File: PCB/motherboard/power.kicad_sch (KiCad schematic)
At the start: 40 parts, among them U1 TPS54140ADGQR, U2 PTPS259830LNRGER, U3 AP2112K-3.3TRG1

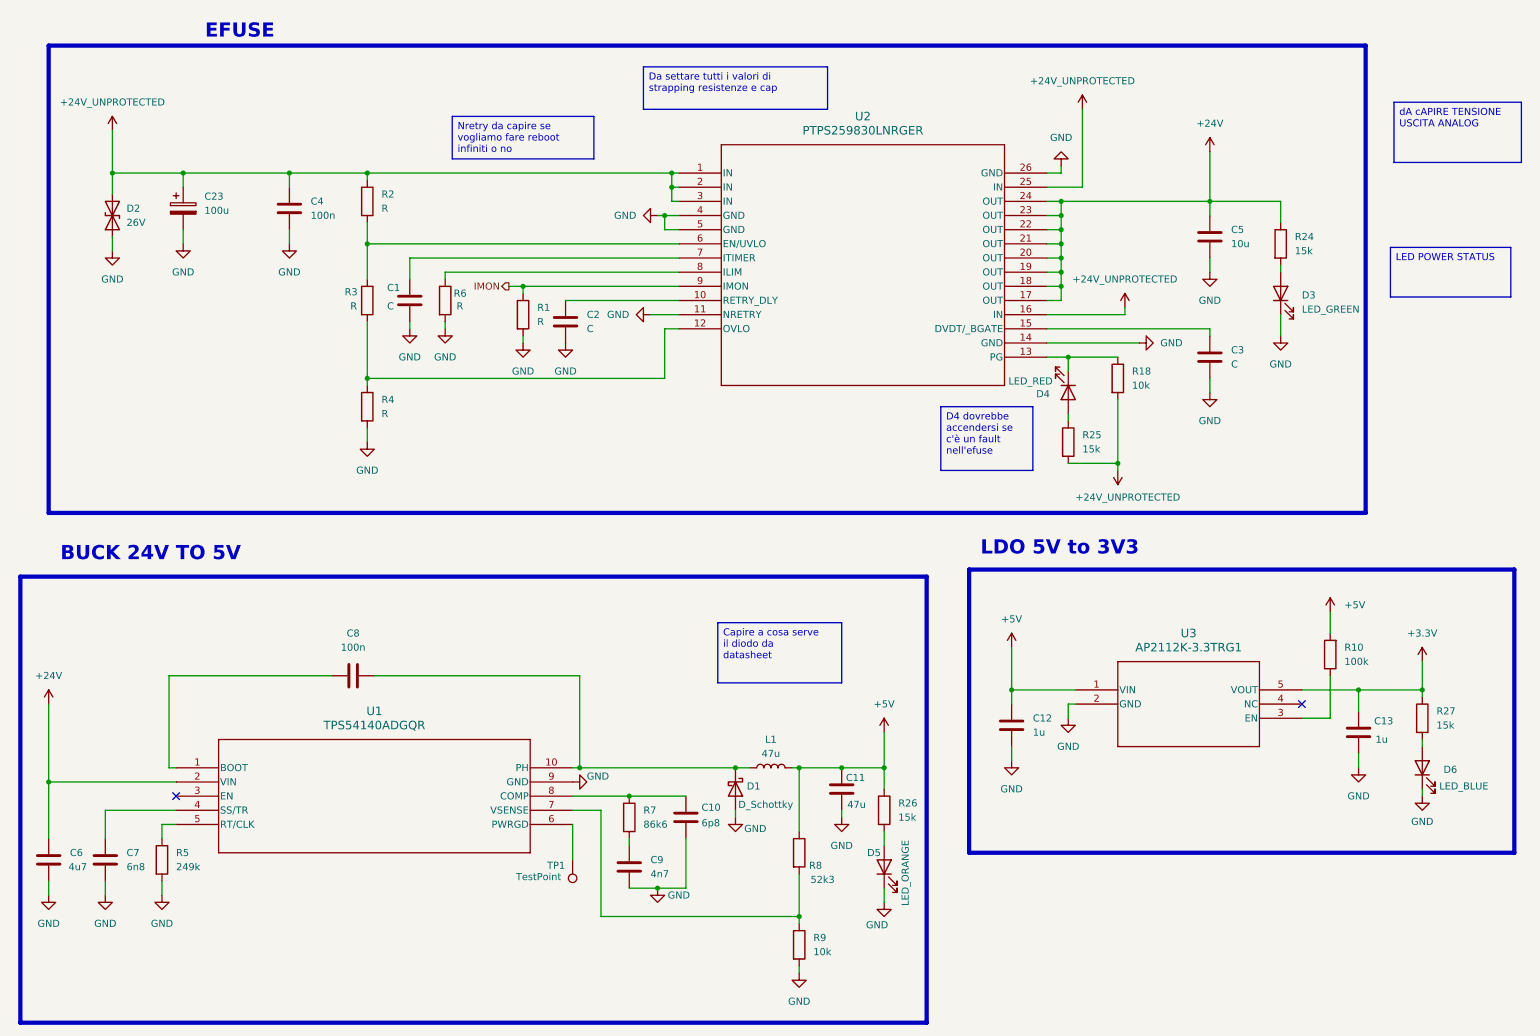
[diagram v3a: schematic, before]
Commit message: schematics need only sizing
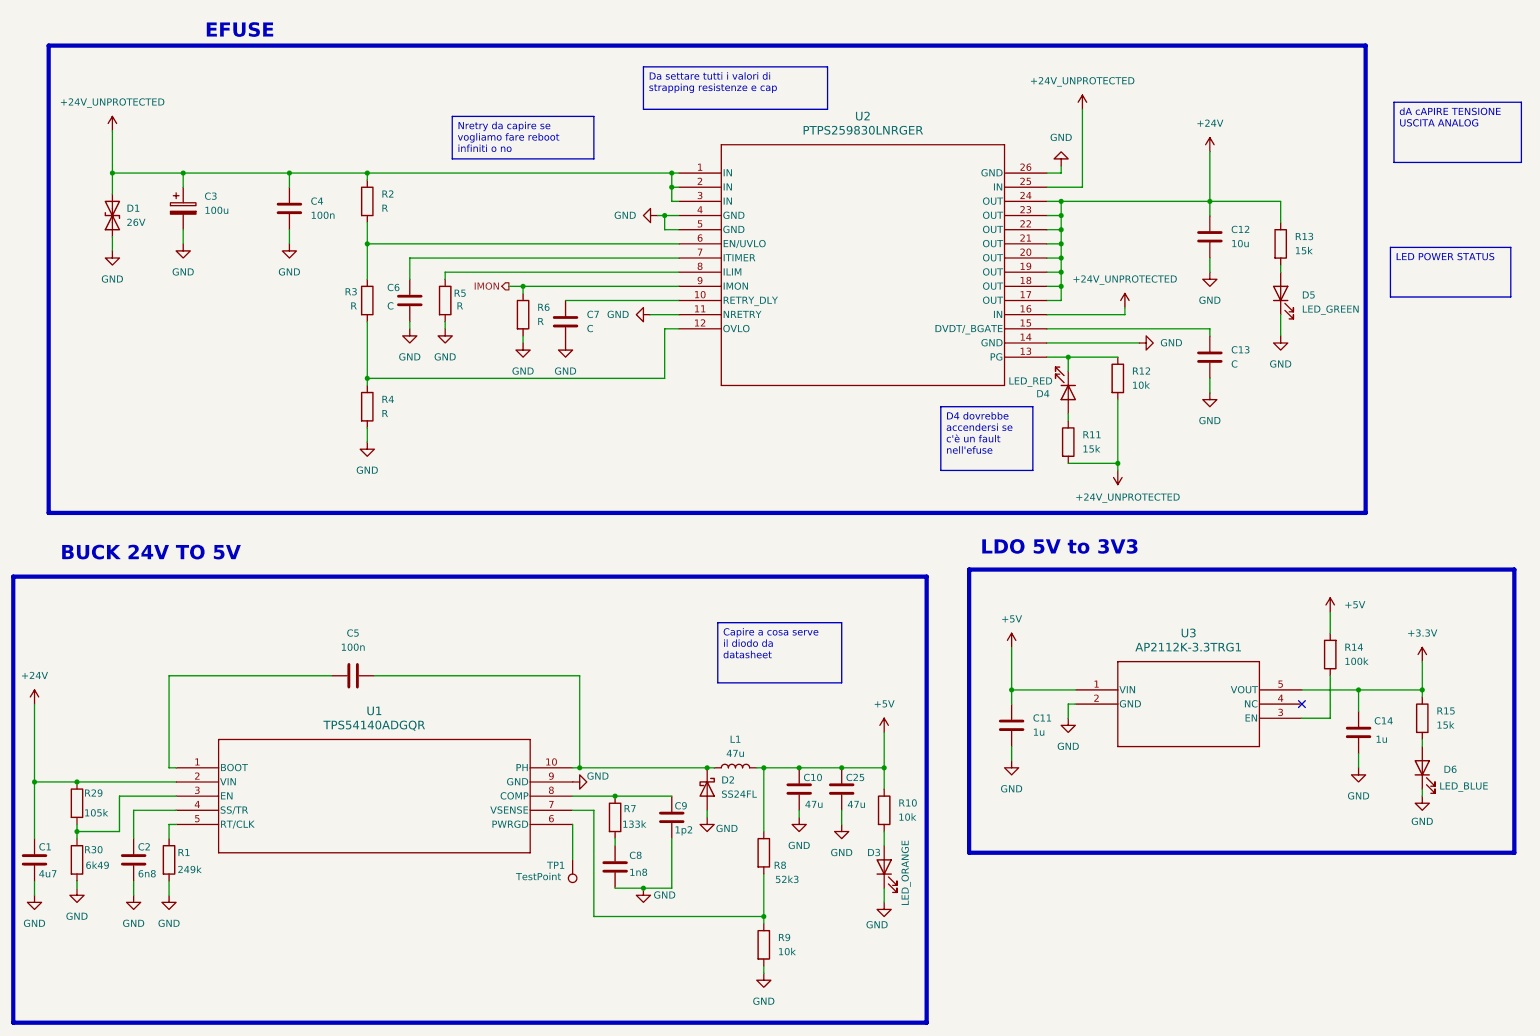
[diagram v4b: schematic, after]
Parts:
- removed D1: D_Schottky, symbol Device:D_Schottky
- added C25: 47u, Capacitor_SMD:C_1206_3216Metric_Pad1.33x1.80mm_HandSolder, symbol Device:C
- added D2: SS24FL, Diode_SMD:D_SMA, symbol Diode:SS24
- added R29: 105k, Resistor_SMD:R_1206_3216Metric_Pad1.30x1.75mm_HandSolder, symbol Device:R
- added R30: 6k49, Resistor_SMD:R_1206_3216Metric_Pad1.30x1.75mm_HandSolder, symbol Device:R
- C1: renamed from C6; footprint (none) -> Capacitor_SMD:C_1206_3216Metric_Pad1.33x1.80mm_HandSolder
- C10: renamed from C11; footprint (none) -> Capacitor_SMD:C_1206_3216Metric_Pad1.33x1.80mm_HandSolder
- C11: renamed from C12; footprint (none) -> Capacitor_SMD:C_1206_3216Metric_Pad1.33x1.80mm_HandSolder
- C12: renamed from C5; footprint (none) -> Capacitor_SMD:C_1206_3216Metric_Pad1.33x1.80mm_HandSolder
- C13: renamed from C3; footprint (none) -> Capacitor_SMD:C_1206_3216Metric_Pad1.33x1.80mm_HandSolder
- C14: renamed from C13; footprint (none) -> Capacitor_SMD:C_1206_3216Metric_Pad1.33x1.80mm_HandSolder
- C2: renamed from C7; footprint (none) -> Capacitor_SMD:C_1206_3216Metric_Pad1.33x1.80mm_HandSolder
- C3: renamed from C23; footprint (none) -> Capacitor_SMD:C_1206_3216Metric_Pad1.33x1.80mm_HandSolder
- C4: footprint (none) -> Capacitor_SMD:C_1206_3216Metric_Pad1.33x1.80mm_HandSolder
- C5: renamed from C8; footprint (none) -> Capacitor_SMD:C_1206_3216Metric_Pad1.33x1.80mm_HandSolder
- C6: renamed from C1; footprint (none) -> Capacitor_SMD:C_1206_3216Metric_Pad1.33x1.80mm_HandSolder
- C7: renamed from C2; footprint (none) -> Capacitor_SMD:C_1206_3216Metric_Pad1.33x1.80mm_HandSolder
- C8: renamed from C9; value 4n7 -> 1n8; footprint (none) -> Capacitor_SMD:C_1206_3216Metric_Pad1.33x1.80mm_HandSolder
- C9: renamed from C10; value 6p8 -> 1p2; footprint (none) -> Capacitor_SMD:C_1206_3216Metric_Pad1.33x1.80mm_HandSolder
- D3: renamed from D5; footprint (none) -> LED_SMD:LED_1206_3216Metric_Pad1.42x1.75mm_HandSolder
- D4, D6: footprint (none) -> LED_SMD:LED_1206_3216Metric_Pad1.42x1.75mm_HandSolder
- D5: renamed from D3; footprint (none) -> LED_SMD:LED_1206_3216Metric_Pad1.42x1.75mm_HandSolder
- R1: renamed from R5; footprint (none) -> Resistor_SMD:R_1206_3216Metric_Pad1.30x1.75mm_HandSolder
- R10: renamed from R26; value 15k -> 10k; footprint (none) -> Resistor_SMD:R_1206_3216Metric_Pad1.30x1.75mm_HandSolder
- R11: renamed from R25; footprint (none) -> Resistor_SMD:R_1206_3216Metric_Pad1.30x1.75mm_HandSolder
- R12: renamed from R18; footprint (none) -> Resistor_SMD:R_1206_3216Metric_Pad1.30x1.75mm_HandSolder
- R13: renamed from R24; footprint (none) -> Resistor_SMD:R_1206_3216Metric_Pad1.30x1.75mm_HandSolder
- R14: renamed from R10; footprint (none) -> Resistor_SMD:R_1206_3216Metric_Pad1.30x1.75mm_HandSolder
- R15: renamed from R27; footprint (none) -> Resistor_SMD:R_1206_3216Metric_Pad1.30x1.75mm_HandSolder
- R2, R3, R4, R8, R9: footprint (none) -> Resistor_SMD:R_1206_3216Metric_Pad1.30x1.75mm_HandSolder
- R5: renamed from R6; footprint (none) -> Resistor_SMD:R_1206_3216Metric_Pad1.30x1.75mm_HandSolder
- R6: renamed from R1; footprint (none) -> Resistor_SMD:R_1206_3216Metric_Pad1.30x1.75mm_HandSolder
- R7: value 86k6 -> 133k; footprint (none) -> Resistor_SMD:R_1206_3216Metric_Pad1.30x1.75mm_HandSolder
- TP1: footprint (none) -> TestPoint:TestPoint_Pad_D2.5mm
- U1: footprint DGQ10_1P88X1P57_TEX -> dgq10:DGQ10_1P88X1P57_TEX
- U2: footprint VQFN24_RGE_TEX -> vqfn24:VQFN24_RGE_TEX
- U3: footprint SOT_RG1_DIO -> SOT_RG1:SOT_RG1_DIO
- renumbered D2 to D1
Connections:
- net +24V: now also R29.1
- net +5V: now also C25.1
- net GND: now also C25.2, D2.2 (A), R30.2
- net at C5.2, L1.1, U1.10 (PH): now also D2.1 (K)
- net at U1.3 (EN): now also R29.2, R30.1
- no-connect marks 2 -> 1
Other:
- moved on the sheet: C1, C10, C2, C8, C9, L1, R1, R7, R8, R9

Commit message: sizing schematics done
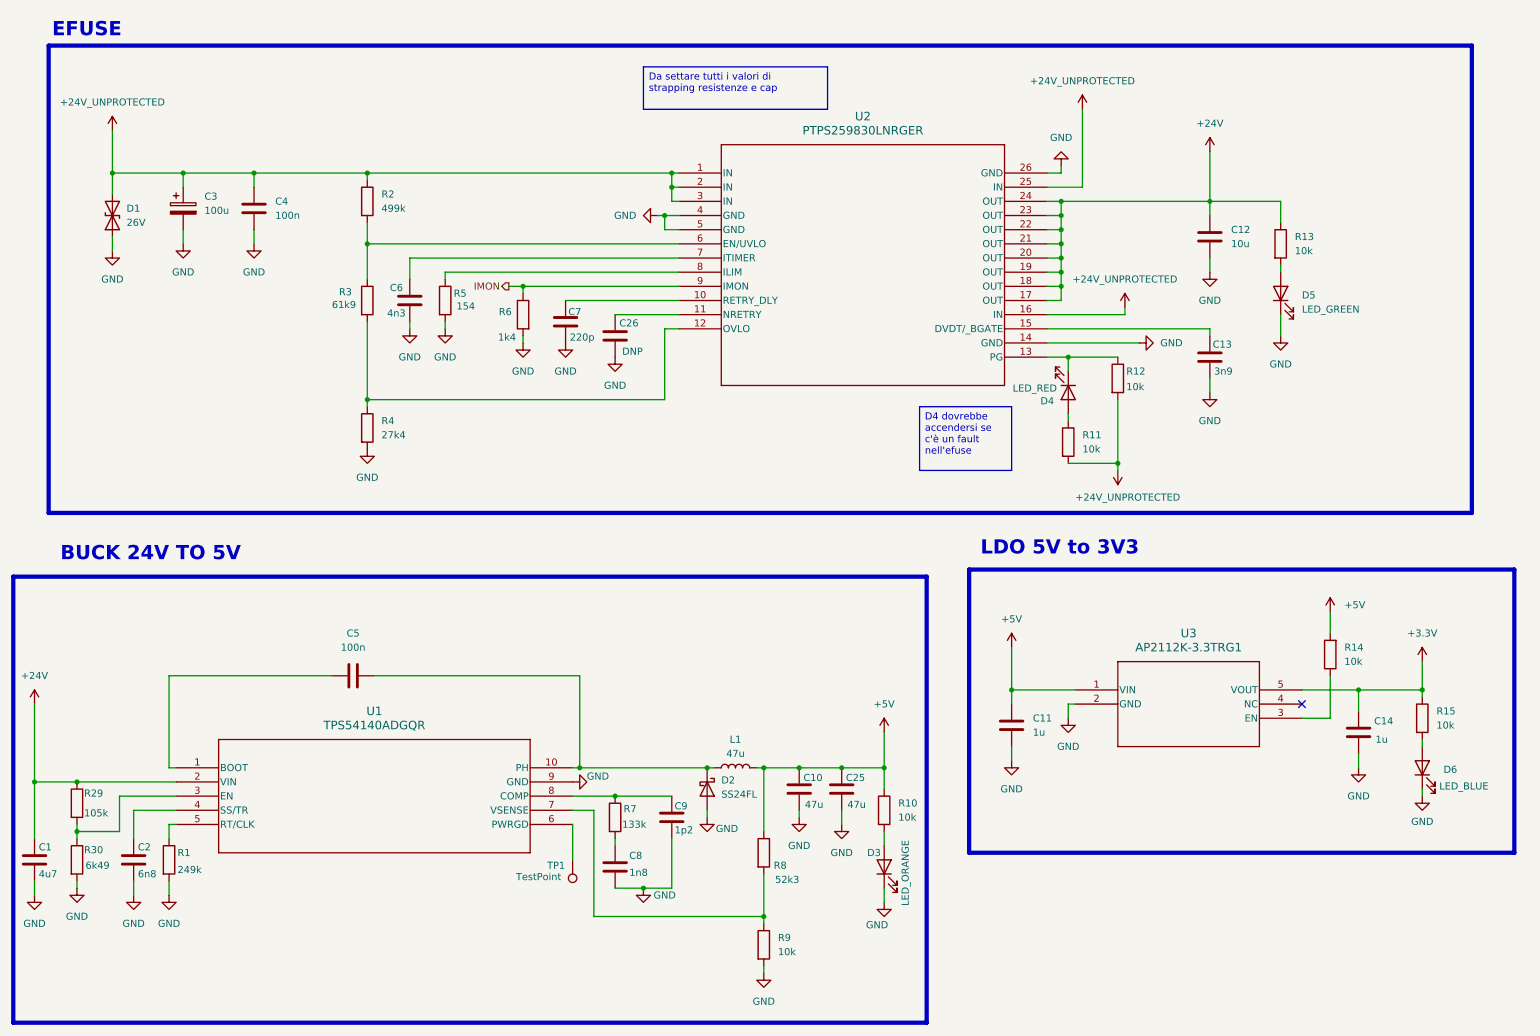
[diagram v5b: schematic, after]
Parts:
- added C26: DNP, Capacitor_SMD:C_1206_3216Metric_Pad1.33x1.80mm_HandSolder, symbol Device:C
- C13: value C -> 3n9
- C6: value C -> 4n3
- C7: value C -> 220p
- R11, R13, R15: value 15k -> 10k
- R14: value 100k -> 10k
- R2: value R -> 499k
- R3: value R -> 61k9
- R4: value R -> 27k4
- R5: value R -> 154
- R6: value R -> 1k4
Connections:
- net GND: now also C26.2; no longer U2.11 (NRETRY)
- new net: C26.1, U2.11 (NRETRY)
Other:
- moved on the sheet: C4, R4

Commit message: added last footprint on sch
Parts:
- D1: footprint (none) -> diodes:SMB_L4.3-W3.6-LS5.4-BI
- D2: footprint Diode_SMD:D_SMA -> diodes:SMA_L4.4-W2.8-LS5.4-RD
- L1: footprint (none) -> inductors:IND-SMD_L7.3-W6.8
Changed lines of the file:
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@@
 			)
 		)
-		(property "Footprint" ""
+		(property "Footprint" "inductors:IND-SMD_L7.3-W6.8"
 			(at 142.24 147.32 0)
 			(hide yes)
@@
 			)
 		)
-		(property "Footprint" "Diode_SMD:D_SMA"
+		(property "Footprint" "diodes:SMA_L4.4-W2.8-LS5.4-RD"
 			(at 132.715 151.13 0)
 			(hide yes)
@@
 			)
 		)
-		(property "Footprint" ""
+		(property "Footprint" "diodes:SMB_L4.3-W3.6-LS5.4-BI"
 			(at 30.48 48.26 0)
 			(hide yes)

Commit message: pcb layout
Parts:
- C1, C12, C13, C2, C26, C4, C5, C6, C7, C8, C9: VRATE (none) -> 50
- C10, C25: VRATE (none) -> 10
- C11, C14: VRATE (none) -> 16
- C3: footprint Capacitor_SMD:C_1206_3216Metric_Pad1.33x1.80mm_HandSolder -> Capacitor_SMD:C_Elec_10x10.2; VRATE (none) -> 50
- L1: footprint inductors:IND-SMD_L7.3-W6.8 -> inductors:IND-SMD_L13.5-W12.6_125CDMCC-DS
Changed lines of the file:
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@@
 			)
 		)
+		(property "VRATE" "50"
+			(at 34.29 163.83 0)
+			(hide yes)
+			(show_name no)
+			(do_not_autoplace no)
+			(effects
+				(font
+					(size 1.27 1.27)
+				)
+			)
+		)
 		(pin "2"
 		)
@@
 			)
 		)
+		(property "VRATE" "50"
+			(at 16.51 163.83 0)
+			(hide yes)
+			(show_name no)
+			(do_not_autoplace no)
+			(effects
+				(font
+					(size 1.27 1.27)
+				)
+			)
+		)
 		(pin "2"
 		)
@@
 			)
 		)
+		(property "VRATE" "50"
+			(at 73.66 130.81 90)
+			(hide yes)
+			(show_name no)
+			(do_not_autoplace no)
+			(effects
+				(font
+					(size 1.27 1.27)
+				)
+			)
+		)
 		(pin "1"
 		)
@@
 			)
 		)
+		(property "VRATE" "50"
+			(at 55.88 46.99 0)
+			(hide yes)
+			(show_name no)
+			(do_not_autoplace no)
+			(effects
+				(font
+					(size 1.27 1.27)
+				)
+			)
+		)
 		(pin "2"
 		)
@@
 			)
 		)
-		(property "Footprint" "Capacitor_SMD:C_1206_3216Metric_Pad1.33x1.80mm_HandSolder"
+		(property "Footprint" "Capacitor_SMD:C_Elec_10x10.2"
 			(at 44.1452 50.8 0)
 			(hide yes)
@@
 			)
 		)
+		(property "VRATE" "50"
+			(at 43.18 46.99 0)
+			(hide yes)
+			(show_name no)
+			(do_not_autoplace no)
+			(effects
+				(font
+					(size 1.27 1.27)
+				)
+			)
+		)
 		(pin "2"
 		)
@@
 			)
 		)
-		(property "Footprint" "inductors:IND-SMD_L7.3-W6.8"
+		(property "Footprint" "inductors:IND-SMD_L13.5-W12.6_125CDMCC-DS"
 			(at 142.24 147.32 0)
 			(hide yes)
@@
 			)
 		)
+		(property "VRATE" "16"
+			(at 191.77 139.7 0)
+			(hide yes)
+			(show_name no)
+			(do_not_autoplace no)
+			(effects
+				(font
+					(size 1.27 1.27)
+				)
+			)
+		)
 		(pin "1"
 		)
@@
 			)
 		)
+		(property "VRATE" "50"
+			(at 83.82 63.5 0)
+			(hide yes)
+			(show_name no)
+			(do_not_autoplace no)
+			(effects
+				(font
+					(size 1.27 1.27)
+				)
+			)
+		)
 		(pin "2"
 		)
@@
 			)
 		)
+		(property "VRATE" "50"
+			(at 227.33 52.07 0)
+			(hide yes)
+			(show_name no)
+			(do_not_autoplace no)
+			(effects
+				(font
+					(size 1.27 1.27)
+				)
+			)
+		)
 		(pin "2"
 		)
@@
 			)
 		)
+		(property "VRATE" "10"
+			(at 153.67 151.13 0)
+			(hide yes)
+			(show_name no)
+			(do_not_autoplace no)
+			(effects
+				(font
+					(size 1.27 1.27)
+				)
+			)
+		)
 		(pin "1"
 		)
@@
 			)
 		)
+		(property "VRATE" "16"
+			(at 254 140.97 0)
+			(hide yes)
+			(show_name no)
+			(do_not_autoplace no)
+			(effects
+				(font
+					(size 1.27 1.27)
+				)
+			)
+		)
 		(pin "1"
 		)
@@
 			)
 		)
+		(property "VRATE" "50"
+			(at 227.33 73.66 0)
+			(hide yes)
+			(show_name no)
+			(do_not_autoplace no)
+			(effects
+				(font
+					(size 1.27 1.27)
+				)
+			)
+		)
 		(pin "2"
 		)
@@
 			)
 		)
+		(property "VRATE" "50"
+			(at 130.81 156.21 0)
+			(hide yes)
+			(show_name no)
+			(do_not_autoplace no)
+			(effects
+				(font
+					(size 1.27 1.27)
+				)
+			)
+		)
 		(pin "2"
 		)
@@
 			)
 		)
+		(property "VRATE" "50"
+			(at 120.65 69.85 0)
+			(hide yes)
+			(show_name no)
+			(do_not_autoplace no)
+			(effects
+				(font
+					(size 1.27 1.27)
+				)
+			)
+		)
 		(pin "1"
 		)
@@
 			)
 		)
+		(property "VRATE" "10"
+			(at 161.29 151.13 0)
+			(hide yes)
+			(show_name no)
+			(do_not_autoplace no)
+			(effects
+				(font
+					(size 1.27 1.27)
+				)
+			)
+		)
 		(pin "1"
 		)
@@
 			)
 		)
+		(property "VRATE" "50"
+			(at 120.65 165.1 0)
+			(hide yes)
+			(show_name no)
+			(do_not_autoplace no)
+			(effects
+				(font
+					(size 1.27 1.27)
+				)
+			)
+		)
 		(pin "1"
 		)
@@
 			(at 111.76 67.31 0)
 			(hide yes)
+			(show_name no)
+			(do_not_autoplace no)
+			(effects
+				(font
+					(size 1.27 1.27)
+				)
+			)
+		)
+		(property "VRATE" "50"
+			(at 111.76 67.31 0)
+			(hide yes)

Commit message: resolved pcb errors from drc, generated test output files
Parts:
- C26: now left out of the parts list
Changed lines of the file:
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@@
 		(body_style 1)
 		(exclude_from_sim no)
-		(in_bom yes)
+		(in_bom no)
 		(on_board yes)
 		(in_pos_files yes)
